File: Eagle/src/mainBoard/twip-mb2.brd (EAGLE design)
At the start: 82.2 x 82.5 mm, 19 parts, among them U1 GY-521MPU6050

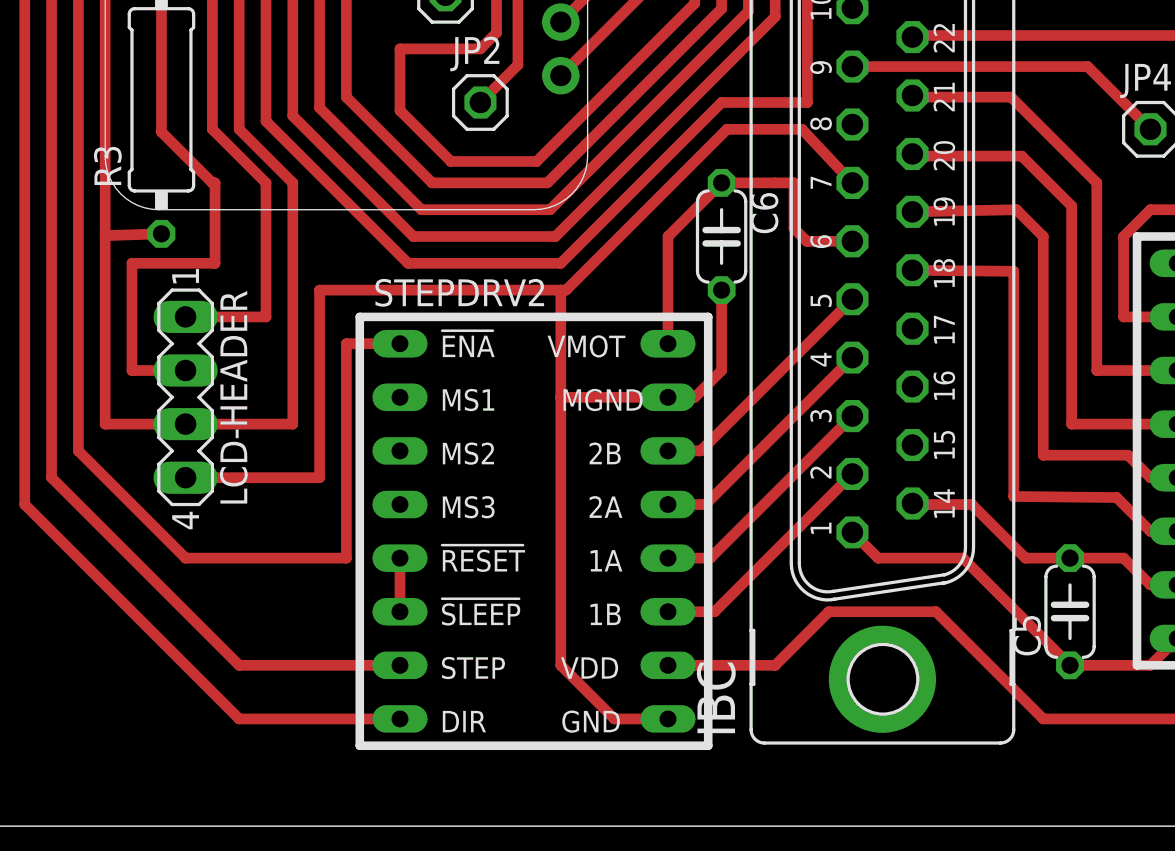
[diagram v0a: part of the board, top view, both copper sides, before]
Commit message: Update twip-mb2.brd
change MB2 LCD header wiring to match order of LCD 1602 I2C interface
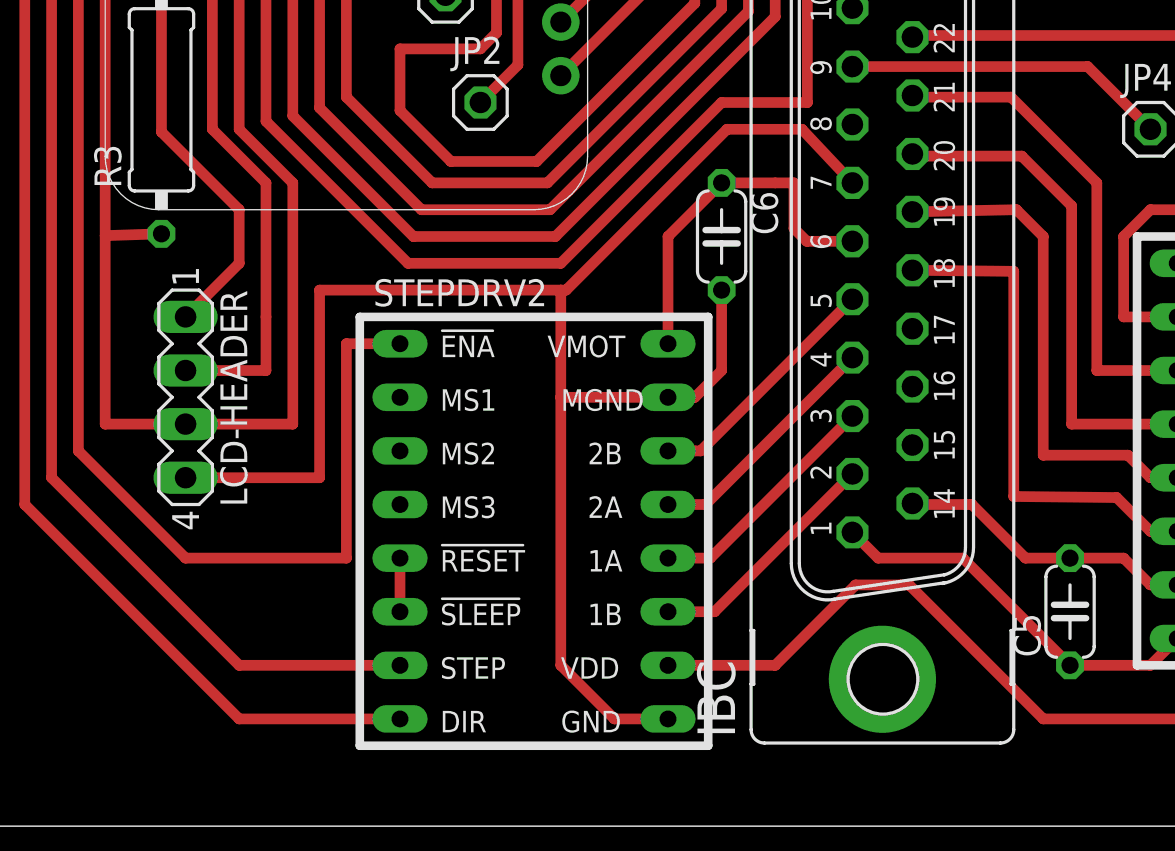
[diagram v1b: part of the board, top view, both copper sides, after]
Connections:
- net N$11: now also LCD-HEADER.1; no longer LCD-HEADER.2
- net N$35: now also LCD-HEADER.2; no longer LCD-HEADER.1
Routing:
- net N$11: track 57.9 -> 50.3 mm
- net N$35: track 59.6 -> 62.1 mm
- net 3V: track 304.4 -> 305.4 mm
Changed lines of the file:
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@@
 <wire x1="30.48" y1="38.1" x2="34.29" y2="41.91" width="0.508" layer="1"/>
 <wire x1="34.29" y1="41.91" x2="34.29" y2="63.5" width="0.508" layer="1"/>
-<wire x1="40.64" y1="7.62" x2="43.18" y2="10.16" width="0.508" layer="1"/>
-<wire x1="43.18" y1="10.16" x2="48.26" y2="10.16" width="0.508" layer="1"/>
-<wire x1="48.26" y1="10.16" x2="53.34" y2="5.08" width="0.508" layer="1"/>
+<wire x1="40.64" y1="7.62" x2="44.45" y2="11.43" width="0.508" layer="1"/>
+<wire x1="44.45" y1="11.43" x2="46.99" y2="11.43" width="0.508" layer="1"/>
+<wire x1="46.99" y1="11.43" x2="53.34" y2="5.08" width="0.508" layer="1"/>
 <wire x1="17.78" y1="80.01" x2="60.96" y2="80.01" width="0.508" layer="1"/>
 <wire x1="64.77" y1="76.2" x2="64.77" y2="71.12" width="0.508" layer="1"/>
@@
 <wire x1="13.97" y1="44.958" x2="11.557" y2="42.545" width="0.508" layer="1"/>
 <wire x1="11.557" y1="42.545" x2="11.557" y2="40.767" width="0.508" layer="1"/>
-<wire x1="14.097" y1="30.48" x2="14.097" y2="26.67" width="0.508" layer="1"/>
 <wire x1="11.557" y1="40.767" x2="11.557" y2="32.893" width="0.508" layer="1"/>
-<wire x1="11.557" y1="32.893" x2="13.97" y2="30.48" width="0.508" layer="1"/>
-<wire x1="13.97" y1="30.48" x2="14.097" y2="30.48" width="0.508" layer="1"/>
 <contactref element="MS2" pad="19"/>
 <wire x1="10.16" y1="68.58" x2="11.43" y2="68.58" width="0.508" layer="1"/>
@@
 <wire x1="13.97" y1="52.07" x2="12.7" y2="53.34" width="0.508" layer="1"/>
 <wire x1="12.7" y1="53.34" x2="12.7" y2="67.31" width="0.508" layer="1"/>
-<wire x1="14.097" y1="26.67" x2="10.16" y2="26.67" width="0.508" layer="1"/>
-<contactref element="LCD-HEADER" pad="2"/>
-<wire x1="10.16" y1="26.67" x2="10.16" y2="21.59" width="0.508" layer="1"/>
-<wire x1="10.16" y1="21.59" x2="12.7" y2="21.59" width="0.508" layer="1"/>
+<contactref element="LCD-HEADER" pad="1"/>
+<wire x1="11.557" y1="32.893" x2="15.24" y2="29.21" width="0.508" layer="1"/>
+<wire x1="15.24" y1="29.21" x2="15.24" y2="26.67" width="0.508" layer="1"/>
+<wire x1="15.24" y1="26.67" x2="12.7" y2="24.13" width="0.508" layer="1"/>
 </signal>
 <signal name="N$33">
@@
 <wire x1="13.97" y1="58.293" x2="17.78" y2="58.293" width="0.508" layer="1"/>
 <wire x1="17.78" y1="55.88" x2="17.78" y2="58.293" width="0.508" layer="1"/>
-<contactref element="LCD-HEADER" pad="1"/>
-<wire x1="12.7" y1="24.13" x2="16.51" y2="24.13" width="0.508" layer="1"/>
+<contactref element="LCD-HEADER" pad="2"/>
+<wire x1="16.51" y1="24.13" x2="16.51" y2="21.59" width="0.508" layer="1"/>
+<wire x1="16.51" y1="21.59" x2="12.7" y2="21.59" width="0.508" layer="1"/>
 </signal>
 <signal name="N$19">
